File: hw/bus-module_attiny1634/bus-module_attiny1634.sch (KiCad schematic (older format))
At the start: 30 parts, among them J1 CONN_5X2, J2 CONN_5X2, J3 CONN-ISP-6, J4 CONN_1, J5 CONN_1, J6 CONN_1, J7 CONN_1, U1 7,3728MHz, U2 25LCXXX, U3 ATtiny1634-SOIC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

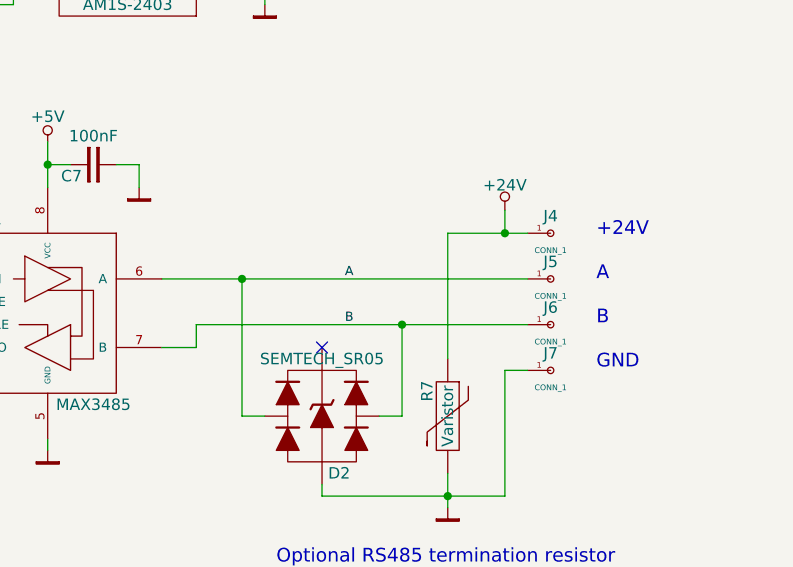
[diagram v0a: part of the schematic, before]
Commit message: Start of development of Rev. B: - integrated fuse for 24V supply. - new footprint SOT143 for TVS-Diode. - replaced TVS-Diode footprint by SOT143. - added revision text on copper layer.
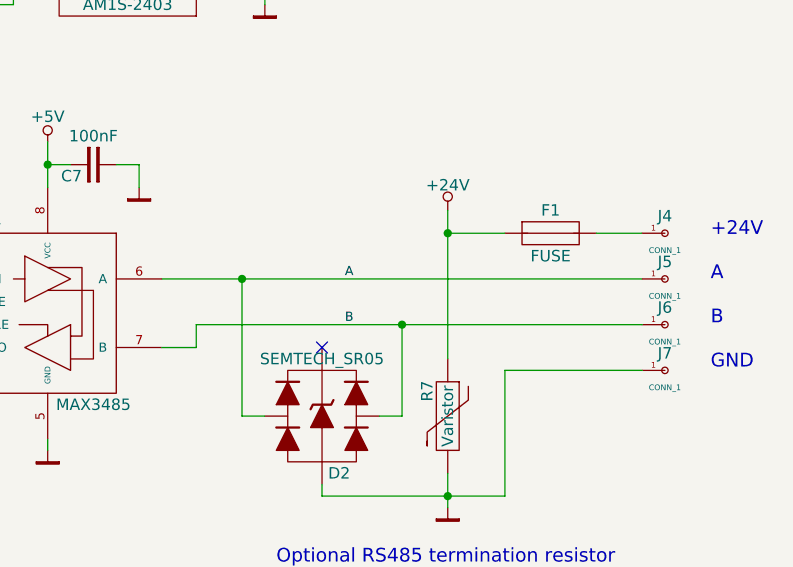
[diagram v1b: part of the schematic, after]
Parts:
- added F1: FUSE, Resistor:R_1812, symbol FUSE
- D2: footprint Housings_SOT:SOT143R_Diode_Reverse -> Diode_SMD:SOT143
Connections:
- net +24V: now also F1.1; no longer J4.1
- new net: F1.2, J4.1
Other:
- moved on the sheet: J4, J5, J6, J7
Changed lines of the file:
@@
 LIBS:connectors
 LIBS:diodes
+LIBS:logo
 LIBS:ics_controller_atmel
 LIBS:ics_misc
 LIBS:ics_peripheral
-LIBS:ics_regulator
-LIBS:logo
+LIBS:ics_signal
 LIBS:power
 LIBS:standard
+LIBS:transistors
 LIBS:bus-module_attiny1634-cache
 EELAYER 25 0
@@
 Sheet 1 1
 Title "bus-module_attiny1634"
-Date "2015-10-28"
-Rev "1"
+Date "2015-12-06"
+Rev "2"
 Comp "KoeWiBa"
 Comment1 ""
@@
 L CONN_1 J4
 U 1 1 559D5A6B
-P 9900 2500
-F 0 "J4" H 9900 2575 50  0000 C CNN
-F 1 "CONN_1" H 9900 2425 25  0000 C CNN
-F 2 "Connector_Miscelleaneus:WAGO243" H 9900 2500 60  0001 C CNN
-F 3 "" H 9900 2500 60  0000 C CNN
-	1    9900 2500
+P 10400 2500
+F 0 "J4" H 10400 2575 50  0000 C CNN
+F 1 "CONN_1" H 10400 2425 25  0000 C CNN
+F 2 "Connector_Miscelleaneus:WAGO243" H 10400 2500 60  0001 C CNN
+F 3 "" H 10400 2500 60  0000 C CNN
+	1    10400 2500
 	1    0    0    -1
 $EndComp
@@
 L CONN_1 J5
 U 1 1 559D5ACC
-P 9900 2700
-F 0 "J5" H 9900 2775 50  0000 C CNN
-F 1 "CONN_1" H 9900 2625 25  0000 C CNN
-F 2 "Connector_Miscelleaneus:WAGO243" H 9900 2700 60  0001 C CNN
-F 3 "" H 9900 2700 60  0000 C CNN
-	1    9900 2700
+P 10400 2700
+F 0 "J5" H 10400 2775 50  0000 C CNN
+F 1 "CONN_1" H 10400 2625 25  0000 C CNN
+F 2 "Connector_Miscelleaneus:WAGO243" H 10400 2700 60  0001 C CNN
+F 3 "" H 10400 2700 60  0000 C CNN
+	1    10400 2700
 	1    0    0    -1
 $EndComp
@@
 L CONN_1 J6
 U 1 1 559D5B5B
-P 9900 2900
-F 0 "J6" H 9900 2975 50  0000 C CNN
-F 1 "CONN_1" H 9900 2825 25  0000 C CNN
-F 2 "Connector_Miscelleaneus:WAGO243" H 9900 2900 60  0001 C CNN
-F 3 "" H 9900 2900 60  0000 C CNN
-	1    9900 2900
+P 10400 2900
+F 0 "J6" H 10400 2975 50  0000 C CNN
+F 1 "CONN_1" H 10400 2825 25  0000 C CNN
+F 2 "Connector_Miscelleaneus:WAGO243" H 10400 2900 60  0001 C CNN
+F 3 "" H 10400 2900 60  0000 C CNN
+	1    10400 2900
 	1    0    0    -1
 $EndComp
@@
 L CONN_1 J7
 U 1 1 559D5B94
-P 9900 3100
-F 0 "J7" H 9900 3175 50  0000 C CNN
-F 1 "CONN_1" H 9900 3025 25  0000 C CNN
-F 2 "Connector_Miscelleaneus:WAGO243" H 9900 3100 60  0001 C CNN
-F 3 "" H 9900 3100 60  0000 C CNN
-	1    9900 3100
+P 10400 3100
+F 0 "J7" H 10400 3175 50  0000 C CNN
+F 1 "CONN_1" H 10400 3025 25  0000 C CNN
+F 2 "Connector_Miscelleaneus:WAGO243" H 10400 3100 60  0001 C CNN
+F 3 "" H 10400 3100 60  0000 C CNN
+	1    10400 3100
 	1    0    0    -1
 $EndComp
@@
 L +24V #PWR03
 U 1 1 559D77F1
-P 9700 2400
-F 0 "#PWR03" H 9700 2600 50  0001 C CNN
-F 1 "+24V" H 9700 2510 50  0000 C CNN
-F 2 "" H 9700 2400 60  0000 C CNN
-F 3 "" H 9700 2400 60  0000 C CNN
-	1    9700 2400
+P 9450 2400
+F 0 "#PWR03" H 9450 2600 50  0001 C CNN
+F 1 "+24V" H 9450 2510 50  0000 C CNN
+F 2 "" H 9450 2400 60  0000 C CNN
+F 3 "" H 9450 2400 60  0000 C CNN
+	1    9450 2400
 	1    0    0    -1
 $EndComp
@@
 	1    0    0    -1
 $EndComp
-Text Notes 10100 3100 0    60   ~ 0
+Text Notes 10600 3100 0    60   ~ 0
 +24V\n\nA\n\nB \n\nGND
 Entry Wire Line
@@
 	6850 2800 7200 2800
 Wire Wire Line
-	8200 2700 9800 2700
+	8200 2700 10300 2700
 Wire Wire Line
 	8350 2900 8350 3000
@@
 	6750 5800 6750 2750
 Wire Wire Line
-	8350 2900 9800 2900
+	8350 2900 10300 2900
 Wire Wire Line
 	4650 3250 4300 3250
@@
 	7200 1450 7200 1600
 Wire Wire Line
-	9700 2400 9700 2500
-Wire Wire Line
-	9800 3100 9700 3100
+	10300 3100 9700 3100
 Wire Wire Line
 	9700 3100 9700 3650
@@
 Wire Bus Line
 	1550 5800 6750 5800
-Wire Wire Line
-	9450 2500 9800 2500
 Wire Wire Line
 	9450 3550 9450 3700
@@
 $EndComp
 Wire Wire Line
-	9450 2500 9450 3050
-Connection ~ 9700 2500
+	9450 2400 9450 3050
 Wire Wire Line
 	7200 2900 7100 2900
@@
 F 0 "D2" H 8975 3050 50  0000 C CNN
 F 1 "SEMTECH_SR05" H 8900 3550 50  0000 C CNN
-F 2 "Housings_SOT:SOT143R_Diode_Reverse" H 8900 3300 60  0001 C CNN
+F 2 "Diode_SMD:SOT143" H 8900 3300 60  0001 C CNN
 F 3 "" H 8900 3300 60  0000 C CNN
 	1    8900 3300
@@
 Text Label 9000 2900 0    40   ~ 0
 B
+$Comp
+L FUSE F1
+U 1 1 56645547
+P 9900 2500
+F 0 "F1" H 9900 2600 50  0000 C CNN
+F 1 "FUSE" H 9900 2400 50  0000 C CNN
+F 2 "Resistor:R_1812" H 9900 2500 60  0001 C CNN
+F 3 "" H 9900 2500 60  0000 C CNN
+	1    9900 2500
+	1    0    0    -1
+$EndComp
+Wire Wire Line
+	10300 2500 10100 2500
+Wire Wire Line
+	9700 2500 9450 2500
+Connection ~ 9450 2500
 $EndSCHEMATC

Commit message: SPI resistors changed from 1k to 100
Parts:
- R2, R3, R4: value 1k -> 100
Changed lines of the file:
@@
 LIBS:transistors
 LIBS:bus-module_attiny1634-cache
-EELAYER 25 0
+EELAYER 26 0
 EELAYER END
 $Descr A4 11693 8268
@@
 Sheet 1 1
 Title "bus-module_attiny1634"
-Date "2015-12-06"
+Date "2017-02-10"
 Rev "2"
 Comp "KoeWiBa"
@@
 P 4800 5700
 F 0 "R4" H 4100 5700 50  0000 C CNN
-F 1 "1k" H 4800 5700 50  0000 C CNN
+F 1 "100" H 4800 5700 50  0000 C CNN
 F 2 "Resistor:SM0805" H 4800 5700 60  0001 C CNN
 F 3 "" H 4800 5700 60  0000 C CNN
@@
 P 4800 5600
 F 0 "R3" H 4100 5600 50  0000 C CNN
-F 1 "1k" H 4800 5600 50  0000 C CNN
+F 1 "100" H 4800 5600 50  0000 C CNN
 F 2 "Resistor:SM0805" H 4800 5600 60  0001 C CNN
 F 3 "" H 4800 5600 60  0000 C CNN
@@
 P 4800 5500
 F 0 "R2" H 4100 5500 50  0000 C CNN
-F 1 "1k" H 4800 5500 50  0000 C CNN
+F 1 "100" H 4800 5500 50  0000 C CNN
 F 2 "Resistor:SM0805" H 4800 5500 60  0001 C CNN
 F 3 "" H 4800 5500 60  0000 C CNN
